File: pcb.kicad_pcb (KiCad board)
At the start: 2 copper layers, 247.4 x 96.5 mm, 170 parts, among them J0 USB_mini_micro_B, P1 CONN_3X2, P2 CONN_4, SW1.1 Backtick, SW1.10 9, SW1.11 0, SW1.12 -, SW1.13 =, SW1.2 1, SW1.3 2, SW1.4 3, SW1.5 4, SW1.6 5, SW1.7 6, SW1.8 7, SW1.9 8, SW2.1 Tab, SW2.10 I, SW2.11 O, SW2.12 P, SW2.13 /, SW2.2 Q, SW2.3 W, SW2.4 E, SW2.5 R, SW2.6 T, SW2.8 Y, SW2.9 U, SW3.1 Bksp, SW3.10 K, SW3.11 L, SW3.12 ;, SW3.13 Enter, SW3.2 A, SW3.3 S, SW3.4 D, SW3.5 F, SW3.6 G, SW3.7 B, SW3.8 H, SW3.9 J, SW4.7 Fn, SW4A1 LShift, SW4A10 ,, SW4A11 ., SW4A13 RShift, SW4A3 Z, SW4A4 X, SW4A5 C, SW4A6 V, SW4A8 N, SW4A9 M, SW4B1 LShift, SW4B10 ,, SW4B11 ., SW4B12 ., SW4B13 RShift, SW4B2 Z, SW4B3 Z, SW4B4 X, SW4B5 C, SW4B6 V, SW4B8 N, SW4B9 M, SW4C1 LShift, SW4C12 ., SW4C13 RShift, SW4C2 Z, SW5A1 LCtrl, SW5A10 1.5, SW5A12 1.5, SW5A13 1.5, SW5A2 LGUI, SW5A4 LAlt, SW5A7 Space, SW5B1 LCtrl, SW5B10 1.25, SW5B12 1.25, SW5B13 1.25, SW5B2 LGUI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

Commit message: Branch for finalizing the board.
TODO:
Swap to smaller components, finalize pads
Added footprints.pretty
Add RGB underglow
Added schematic library (keenkeeb.lib/dcm)
Remove SPI header (?)
Add test pads (?)
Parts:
- added F1: FUSE, LEDs:LED_0805, B.Cu at (94.2, 101.9)
- added LED1: WS2812b, LEDs:LED_WS2812B-PLCC4, B.Cu at (104.8, 169.1)
- added LED10: WS2812b, LEDs:LED_WS2812B-PLCC4, B.Cu at (104.8, 109.5)
- added LED2: WS2812b, LEDs:LED_WS2812B-PLCC4, B.Cu at (152.4, 169.1)
- added LED3: WS2812b, LEDs:LED_WS2812B-PLCC4, B.Cu at (200.0, 169.1)
- added LED4: WS2812b, LEDs:LED_WS2812B-PLCC4, B.Cu at (247.7, 169.1)
- added LED5: WS2812b, LEDs:LED_WS2812B-PLCC4, B.Cu at (295.3, 169.1)
- added LED6: WS2812b, LEDs:LED_WS2812B-PLCC4, B.Cu at (295.3, 109.5)
- added LED7: WS2812b, LEDs:LED_WS2812B-PLCC4, B.Cu at (247.7, 109.5)
- added LED8: WS2812b, LEDs:LED_WS2812B-PLCC4, B.Cu at (200.0, 109.5)
- added LED9: WS2812b, LEDs:LED_WS2812B-PLCC4, B.Cu at (152.4, 109.5)
- C0, C1, C2, C3, C4, C5, C6, C7: footprint Capacitors_SMD:C_0805_HandSoldering -> Capacitors_SMD:C_0805
- D1: footprint Keyboards:LED_3mm_plusminus -> footprints:LED_3mm_plusminus
- OSC0: footprint keyboard_parts:FA-238 -> footprints:OSC_EpsonFA238_SMD
- P1: moved to F.Cu
- R0, R1, R2, R3, R4: footprint Resistors_SMD:R_0805_HandSoldering -> Resistors_SMD:R_0805
- moved P1 141.3 mm to (200.0, 195.7)
- moved G3 54.7 mm to (192.3, 181.9)
- moved G2 54.5 mm to (201.7, 178.8)
- moved R2 7.85 mm to (98.1, 109.1)
- moved R1 7.77 mm to (95.0, 109.1)
- moved C3 2.97 mm to (89.6, 109.1), turned to 270 degrees
- moved C0 1.99 mm to (102.6, 116.9)
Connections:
- J0 pad 1: VCC -> Net-(F1-Pad2)
- uC0 pad 29: /matrix/Row4 -> /matrix/Row5
- uC0 pad 30: /matrix/Row5 -> /matrix/Row4
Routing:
- net VCC: track 142.7 -> 280.6 mm, vias 5 -> 13
- net Net-(LED5-Pad2): track 0.00 -> 65.1 mm, vias 0 -> 2
- net /microcontroller/MISO: track 58.7 -> 0.00 mm, vias 2 -> 0
- net /microcontroller/SCK: track 49.5 -> 0.00 mm, vias 2 -> 0
- net Net-(LED10-Pad4): track 0.00 -> 48.1 mm, vias 0 -> 2
- net /microcontroller/MOSI: track 46.8 -> 0.00 mm, vias 2 -> 0
- net Net-(LED6-Pad2): track 0.00 -> 45.9 mm, vias 0 -> 2
- net Net-(LED3-Pad2): track 0.00 -> 44.0 mm, vias 0 -> 2
- net Net-(LED2-Pad2): track 0.00 -> 44.0 mm, vias 0 -> 2
- net Net-(LED8-Pad2): track 0.00 -> 44.0 mm, vias 0 -> 2
- net Net-(LED7-Pad2): track 0.00 -> 44.0 mm, vias 0 -> 2
- net Net-(LED1-Pad2): track 0.00 -> 44.0 mm, vias 0 -> 2
- net Net-(LED4-Pad2): track 0.00 -> 44.0 mm, vias 0 -> 2
- net /microcontroller/nRST: track 72.4 -> 38.7 mm, vias 3 -> 2
- net Net-(uC0-Pad8): track 14.2 -> 0.00 mm, vias 1 -> 0
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
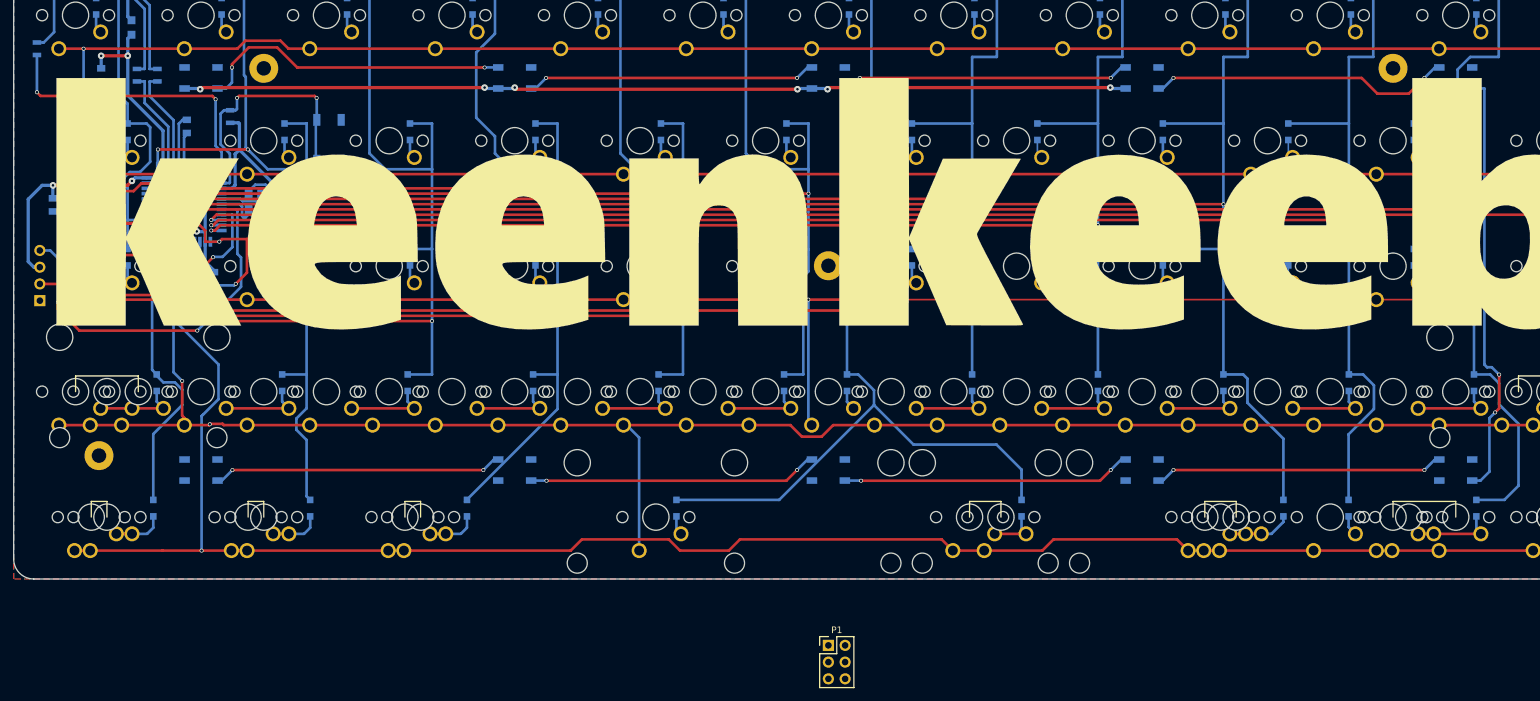
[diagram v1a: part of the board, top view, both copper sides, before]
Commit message: ARR GEE BEE!!!
Added pads for WS2812B underglow - connected to pin 11.
Rerouted some connections.
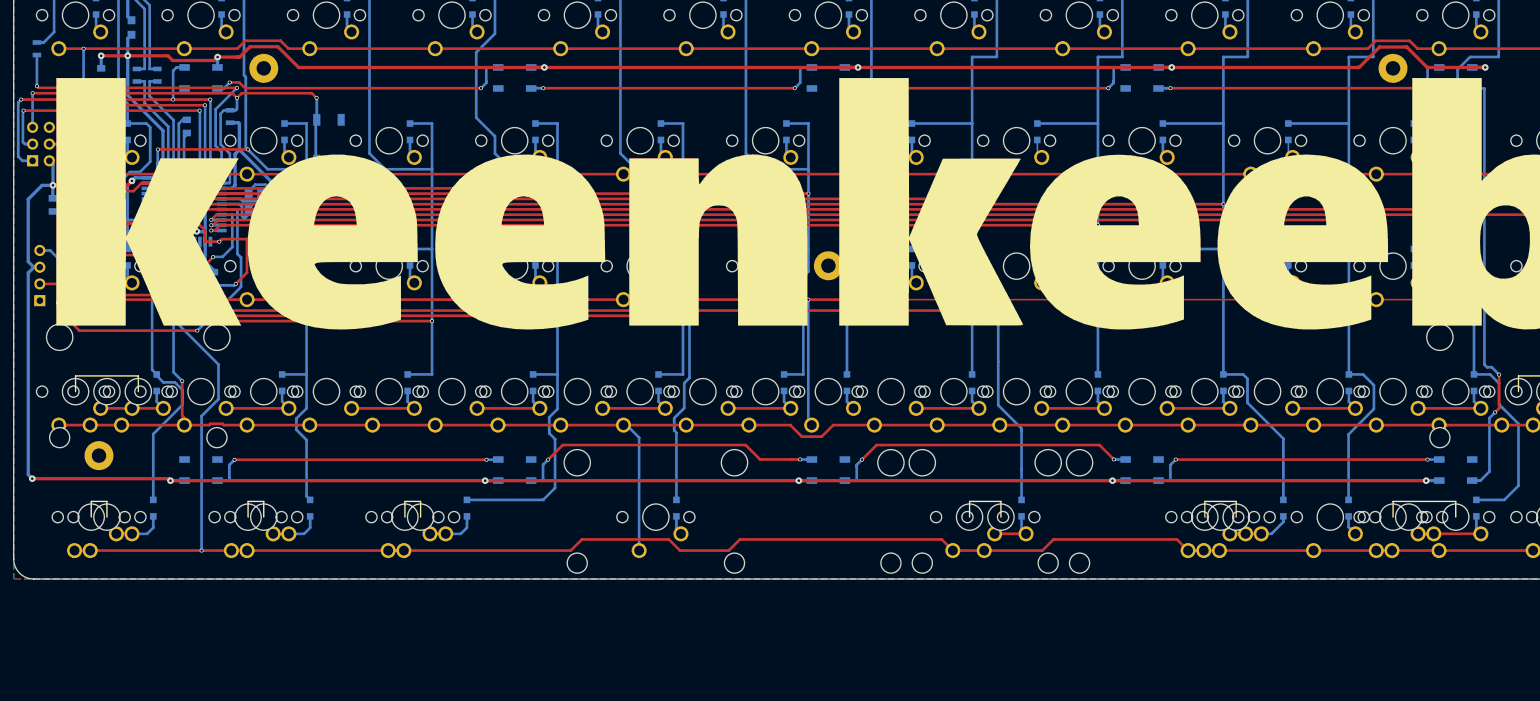
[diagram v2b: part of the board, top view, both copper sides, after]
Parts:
- P1: moved to B.Cu
- moved P1 141.5 mm to (79.2, 122.1)
- turned LED1 to 180 degrees
- turned LED10 to 0 degrees
- turned LED2 to 180 degrees
- turned LED3 to 180 degrees
- turned LED4 to 180 degrees
- turned LED5 to 180 degrees
- turned LED6 to 0 degrees
- turned LED7 to 0 degrees
- turned LED8 to 0 degrees
- turned LED9 to 0 degrees
- renumbered LED10 to LED1, LED1 to LED10, LED9 to LED2, LED8 to LED3, LED7 to LED4, LED6 to LED5, LED5 to LED6, LED4 to LED7, LED3 to LED8, LED2 to LED9
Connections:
- LED1 pad 2: Net-(LED10-Pad2) -> Net-(LED1-Pad2)
- LED1 pad 4: Net-(LED10-Pad4) -> /underglow/Din
- LED10 pad 2: Net-(LED1-Pad2) -> Net-(LED10-Pad2)
- LED10 pad 4: /underglow/Din -> Net-(LED10-Pad4)
- LED2 pad 2: Net-(LED10-Pad4) -> Net-(LED2-Pad2)
- LED2 pad 4: Net-(LED8-Pad2) -> Net-(LED1-Pad2)
- LED3 pad 2: Net-(LED8-Pad2) -> Net-(LED3-Pad2)
- LED3 pad 4: Net-(LED7-Pad2) -> Net-(LED2-Pad2)
- LED4 pad 2: Net-(LED7-Pad2) -> Net-(LED4-Pad2)
- LED4 pad 4: Net-(LED6-Pad2) -> Net-(LED3-Pad2)
- LED5 pad 2: Net-(LED6-Pad2) -> Net-(LED5-Pad2)
- LED5 pad 4: Net-(LED5-Pad2) -> Net-(LED4-Pad2)
- LED6 pad 2: Net-(LED5-Pad2) -> Net-(LED6-Pad2)
- LED6 pad 4: Net-(LED4-Pad2) -> Net-(LED5-Pad2)
- LED7 pad 2: Net-(LED4-Pad2) -> Net-(LED7-Pad2)
- LED7 pad 4: Net-(LED3-Pad2) -> Net-(LED6-Pad2)
- LED8 pad 2: Net-(LED3-Pad2) -> Net-(LED8-Pad2)
- LED8 pad 4: Net-(LED2-Pad2) -> Net-(LED7-Pad2)
- LED9 pad 2: Net-(LED2-Pad2) -> Net-(LED10-Pad4)
- LED9 pad 4: Net-(LED1-Pad2) -> Net-(LED8-Pad2)
- P1 pad 1: /microcontroller/MISO -> /underglow/Din
- uC0 pad 11: /microcontroller/MISO -> /underglow/Din
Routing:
- net VCC: track 280.6 -> 617.3 mm, vias 13 -> 18
- net /underglow/Din: track 0.00 -> 56.5 mm, vias 0 -> 3
- net /microcontroller/SCK: track 0.00 -> 41.7 mm, vias 0 -> 2
- net /microcontroller/MOSI: track 0.00 -> 38.6 mm, vias 0 -> 2
- net /microcontroller/nRST: track 38.7 -> 75.5 mm, vias 2 -> 3
- net /matrix/Col7: track 262.9 -> 253.7 mm, vias 2 -> 4
- net /matrix/Col4: track 176.2 -> 183.4 mm
- net /microcontroller/LED: track 45.5 -> 50.6 mm
- net Net-(LED8-Pad2): track 44.0 -> 47.8 mm
- net Net-(LED7-Pad2): track 44.0 -> 47.2 mm
- net Net-(LED10-Pad4): track 48.1 -> 45.3 mm
- net Net-(LED1-Pad2): track 44.0 -> 46.0 mm
- net Net-(LED3-Pad2): track 44.0 -> 45.4 mm
- net Net-(LED2-Pad2): track 44.0 -> 45.4 mm
- net Net-(LED4-Pad2): track 44.0 -> 45.3 mm
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
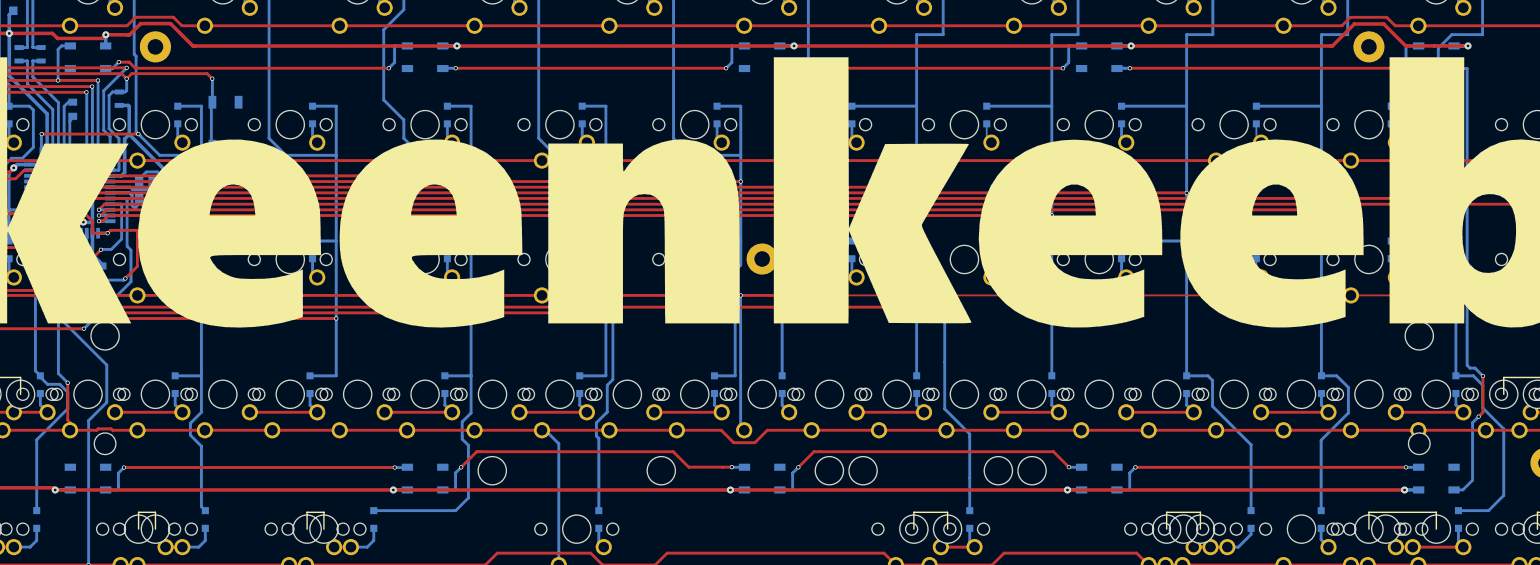
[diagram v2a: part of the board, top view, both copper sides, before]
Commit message: Added 0.1uF caps to LEDs
Added capacitors from Vcc to GND for WS2812s
Also changed some references
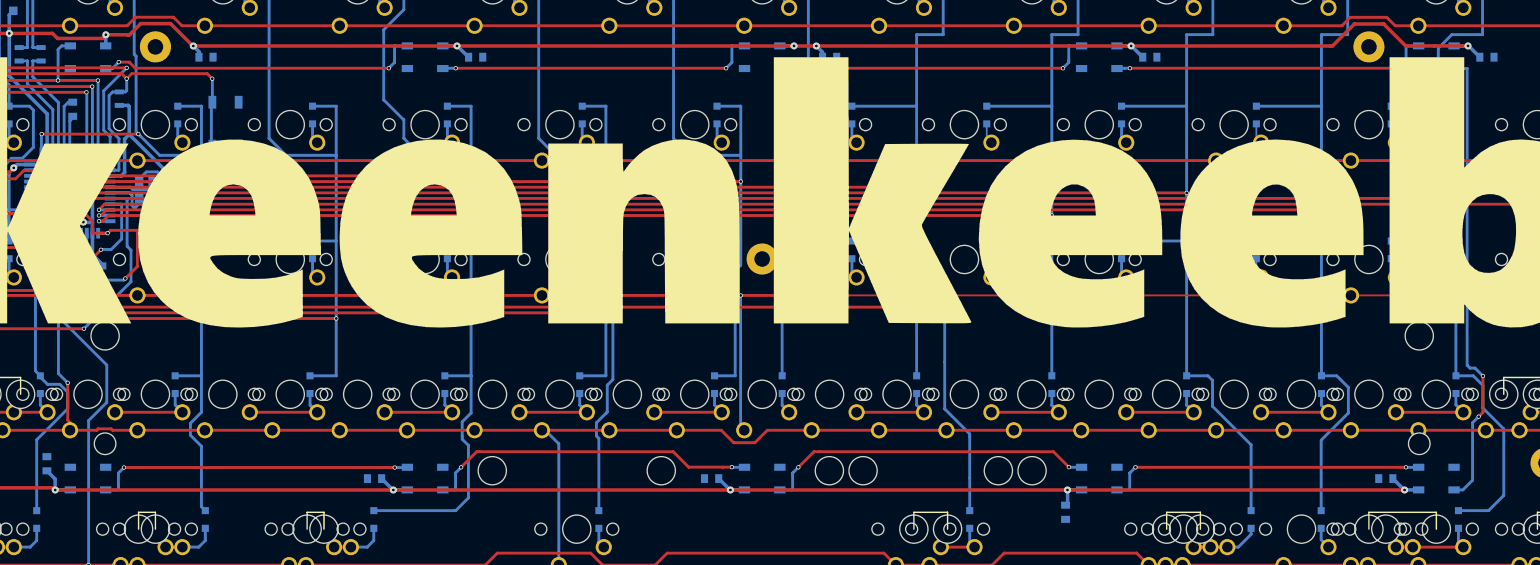
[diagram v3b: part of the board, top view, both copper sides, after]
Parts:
- added C10: 0.1u, Capacitors_SMD:C_0805, B.Cu at (159.5, 109.5)
- added C11: 0.1u, Capacitors_SMD:C_0805, B.Cu at (209.6, 109.5)
- added C12: 0.1u, Capacitors_SMD:C_0805, B.Cu at (254.8, 109.5)
- added C13: 0.1u, Capacitors_SMD:C_0805, B.Cu at (302.4, 109.5)
- added C14: 0.1u, Capacitors_SMD:C_0805, B.Cu at (288.1, 169.1)
- added C15: 0.1u, Capacitors_SMD:C_0805, B.Cu at (242.9, 173.8)
- added C16: 0.1u, Capacitors_SMD:C_0805, B.Cu at (192.9, 169.1)
- added C17: 0.1u, Capacitors_SMD:C_0805, B.Cu at (145.3, 169.1)
- added C18: 0.1u, Capacitors_SMD:C_0805, B.Cu at (99.0, 167.0)
- added C9: 0.1u, Capacitors_SMD:C_0805, B.Cu at (121.4, 109.5)
- renumbered C0 to C1, C1 to C2, C2 to C3, C3 to C4, C4 to C5, C5 to C6, C6 to C7, C7 to C8, R0 to R3, R3 to R4, R4 to R5, uC0 to U1
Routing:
- net VCC: track 617.3 -> 640.6 mm, vias 18 -> 20

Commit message: Moved some of the footprints around.
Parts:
- moved PB0 21.1 mm to (114.7, 100.2), turned to 270 degrees
- moved C9 11.8 mm to (109.8, 107.6), turned to 90 degrees
- moved C7 5.31 mm to (90.4, 128.8)
- moved C15 4.91 mm to (242.0, 169.0), turned to 0 degrees
- moved C11 3.78 mm to (205.8, 109.6)
- moved C18 2.16 mm to (99.1, 169.1), turned to 0 degrees
- moved C16 1.46 mm to (194.3, 169.0)
- moved C17 1.46 mm to (146.7, 169.0)
- moved C14 1.46 mm to (289.6, 169.1)
- moved C10 1.40 mm to (158.1, 109.6)
- moved C12 1.40 mm to (253.4, 109.6)
- moved C13 1.40 mm to (301.0, 109.6)
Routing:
- net VCC: track 640.6 -> 628.3 mm, vias 20 -> 18
- net GND: track 96.5 -> 104.5 mm
- net /matrix/Col8: track 208.3 -> 206.1 mm
- net /matrix/Col9: track 219.7 -> 217.5 mm
- net /matrix/Col11: track 281.3 -> 279.1 mm
- net /matrix/Col12: track 314.3 -> 312.1 mm
- net /matrix/Col10: track 278.7 -> 276.5 mm
- net /matrix/Col13: track 313.1 -> 312.2 mm
- net /microcontroller/nRST: track 75.5 -> 76.4 mm
- net /matrix/Col1: track 99.8 -> 100.4 mm

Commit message: Begun work for rev 1 layout, which supports ortholinear rows 2 and 3.
Converted all switches to use platemount footprint.  Added additional
set of switches to row 3 for a completely ortholinear layout.
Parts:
- removed SW3.1: Bksp, Keyboards:CHERRY_PCB_150H_NoBound
- removed SW3.10: K, Keyboards:CHERRY_PCB_100H_NoBound
- removed SW3.11: L, Keyboards:CHERRY_PCB_100H_NoBound
- removed SW3.12: ;, Keyboards:CHERRY_PCB_100H_NoBound
- removed SW3.13: Enter, Keyboards:CHERRY_PCB_150H_NoBound
- removed SW3.2: A, Keyboards:CHERRY_PCB_100H_NoBound
- removed SW3.3: S, Keyboards:CHERRY_PCB_100H_NoBound
- removed SW3.4: D, Keyboards:CHERRY_PCB_100H_NoBound
- removed SW3.5: F, Keyboards:CHERRY_PCB_100H_NoBound
- removed SW3.6: G, Keyboards:CHERRY_PCB_100H_NoBound
- removed SW3.7: B, Keyboards:CHERRY_PCB_100H_NoBound
- removed SW3.8: H, Keyboards:CHERRY_PCB_100H_NoBound
- removed SW3.9: J, Keyboards:CHERRY_PCB_100H_NoBound
- added SW3A1: Bksp, footprints:MX_150_Plate, F.Cu at (90.5, 138.1)
- added SW3A10: K, footprints:MX_100_Plate, F.Cu at (247.7, 138.1)
- added SW3A11: L, footprints:MX_100_Plate, F.Cu at (266.7, 138.1)
- added SW3A12: ;, footprints:MX_100_Plate, F.Cu at (285.8, 138.1)
- added SW3A13: Enter, footprints:MX_150_Plate, F.Cu at (309.6, 138.1)
- added SW3A2: A, footprints:MX_100_Plate, F.Cu at (114.3, 138.1)
- added SW3A3: S, footprints:MX_100_Plate, F.Cu at (133.3, 138.1)
- added SW3A4: D, footprints:MX_100_Plate, F.Cu at (152.4, 138.1)
- added SW3A5: F, footprints:MX_100_Plate, F.Cu at (171.4, 138.1)
- added SW3A6: G, footprints:MX_100_Plate, F.Cu at (190.5, 138.1)
- added SW3A8: H, footprints:MX_100_Plate, F.Cu at (209.6, 138.1)
- added SW3A9: J, footprints:MX_100_Plate, F.Cu at (228.6, 138.1)
- added SW3B7: B, footprints:MX_100_Plate, F.Cu at (200.0, 138.1)
- SW1.1, SW1.10, SW1.11, SW1.12, SW1.13, SW1.2, SW1.3, SW1.4, SW1.5, SW1.6, SW1.7, SW1.8, SW1.9, SW2.10, SW2.11, SW2.12, SW2.2, SW2.3, SW2.4, SW2.5, SW2.6, SW2.8, SW2.9, SW4A10, SW4A11, SW4A3, SW4A4, SW4A5, SW4A6, SW4A8, SW4A9, SW4B10, SW4B11, SW4B12, SW4B2, SW4B3, SW4B4, SW4B5, SW4B6, SW4B8, SW4B9, SW4C1, SW4C12, SW4C13, SW4C2, SW5A12, SW5A2, SW5C10, SW5C11, SW5C12, SW5C13: footprint Keyboards:CHERRY_PCB_100H_NoBound -> footprints:MX_100_Plate
- SW2.1, SW2.13, SW4B1, SW5A1, SW5A10, SW5A13, SW5A4: footprint Keyboards:CHERRY_PCB_150H_NoBound -> footprints:MX_150_Plate
- SW4.7: footprint Keyboards:CHERRY_PCB_225H_NoBound -> footprints:MX_225_Plate
- SW4A1, SW4A13: footprint Keyboards:CHERRY_PCB_200H_NoBound -> footprints:MX_200_Plate
- SW4B13: footprint Keyboards:CHERRY_PCB_100H_NoBound -> footprints:MX_150_Plate
- SW5A7, SW5B7: footprint Keyboards:CHERRY_PCB_275H_NoBound -> footprints:MX_275_Plate
- SW5B1, SW5B10, SW5B12, SW5B13, SW5B2, SW5B4: footprint Keyboards:CHERRY_PCB_125H_NoBound -> footprints:MX_125_Plate
- moved C13 303.0 mm to (37.9, 259.9)
- moved LED5 295.3 mm to (36.9, 252.6)
- moved Hole5 280.3 mm to (30.6, 177.3)
- moved C8 275.0 mm to (356.4, 106.8)
- moved C12 274.8 mm to (24.1, 261.0)
- moved LED6 269.0 mm to (29.4, 209.9)
- moved R4 265.4 mm to (362.9, 111.6)
- moved LED4 265.2 mm to (24.3, 252.6)
- moved C14 264.5 mm to (29.2, 215.7)
- moved C7 262.9 mm to (352.3, 106.5)
- moved C4 260.4 mm to (350.0, 111.0)
- moved C3 258.9 mm to (372.5, 104.2), turned to 90 degrees
- moved Hole2 258.7 mm to (31.4, 155.5)
- moved OSC0 253.0 mm to (364.8, 103.7), turned to 0 degrees
- moved C2 247.2 mm to (363.0, 97.1)
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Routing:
- net VCC: track 628.3 -> 17.4 mm, vias 18 -> 0
- net /matrix/Col13: track 312.2 -> 97.3 mm, vias 2 -> 0
- net /matrix/Col12: track 312.1 -> 110.2 mm, vias 2 -> 0
- net /matrix/Col11: track 279.1 -> 104.5 mm, vias 2 -> 0
- net /matrix/Col10: track 276.5 -> 112.6 mm, vias 2 -> 0
- net /matrix/Col9: track 217.5 -> 81.0 mm, vias 2 -> 0
- net /matrix/Col8: track 206.1 -> 80.4 mm, vias 2 -> 0
- net /matrix/Col6: track 186.4 -> 85.6 mm, vias 2 -> 0
- net GND: track 104.5 -> 4.10 mm, vias 6 -> 0
- net /matrix/Col7: track 253.7 -> 158.7 mm, vias 4 -> 3
- net /matrix/Col5: track 171.4 -> 86.0 mm, vias 2 -> 0
- net /microcontroller/nRST: track 76.4 -> 0.00 mm, vias 3 -> 0
- net Net-(LED5-Pad2): track 65.1 -> 0.00 mm, vias 2 -> 0
- net /matrix/Col4: track 183.4 -> 120.6 mm, vias 2 -> 0
- net /microcontroller/SCL: track 57.1 -> 0.00 mm, vias 2 -> 0
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
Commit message: Ortholinear switch footprints added to row 2.
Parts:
- added D2.7: D, Diodes_SMD:D_SOD-323_HandSoldering, B.Cu at (204.8, 116.7)
- added SW2B1: Tab, footprints:MX_100_Plate, F.Cu at (85.7, 119.1)
- added SW2B10: I, footprints:MX_100_Plate, F.Cu at (257.2, 119.1)
- added SW2B11: O, footprints:MX_100_Plate, F.Cu at (276.2, 119.1)
- added SW2B12: P, footprints:MX_100_Plate, F.Cu at (295.3, 119.1)
- added SW2B13: /, footprints:MX_100_Plate, F.Cu at (314.3, 119.1)
- added SW2B2: Q, footprints:MX_100_Plate, F.Cu at (104.8, 119.1)
- added SW2B3: W, footprints:MX_100_Plate, F.Cu at (123.8, 119.1)
- added SW2B4: E, footprints:MX_100_Plate, F.Cu at (142.9, 119.1)
- added SW2B5: R, footprints:MX_100_Plate, F.Cu at (161.9, 119.1)
- added SW2B6: T, footprints:MX_100_Plate, F.Cu at (181.0, 119.1)
- added SW2B7: Y, footprints:MX_100_Plate, F.Cu at (200.0, 119.1)
- added SW2B8: Y, footprints:MX_100_Plate, F.Cu at (219.1, 119.1)
- added SW2B9: U, footprints:MX_100_Plate, F.Cu at (238.1, 119.1)
- added SW3B1: Bksp, footprints:MX_100_Plate, F.Cu at (85.7, 138.1)
- added SW3B10: K, footprints:MX_100_Plate, F.Cu at (257.2, 138.1)
- added SW3B11: L, footprints:MX_100_Plate, F.Cu at (276.2, 138.1)
- added SW3B12: ;, footprints:MX_100_Plate, F.Cu at (295.3, 138.1)
- added SW3B13: Enter, footprints:MX_100_Plate, F.Cu at (314.3, 138.1)
- added SW3B2: A, footprints:MX_100_Plate, F.Cu at (104.8, 138.1)
- added SW3B3: S, footprints:MX_100_Plate, F.Cu at (123.8, 138.1)
- added SW3B4: D, footprints:MX_100_Plate, F.Cu at (142.9, 138.1)
- added SW3B5: F, footprints:MX_100_Plate, F.Cu at (161.9, 138.1)
- added SW3B6: G, footprints:MX_100_Plate, F.Cu at (181.0, 138.1)
- added SW3B8: H, footprints:MX_100_Plate, F.Cu at (219.1, 138.1)
- added SW3B9: J, footprints:MX_100_Plate, F.Cu at (238.1, 138.1)
- SW3B7: value B -> H
- moved Hole5 272.1 mm to (302.4, 190.5)
- moved Hole2 265.1 mm to (285.8, 81.0)
- moved Hole1 106.8 mm to (114.3, 81.0)
- moved Hole4 72.6 mm to (100.0, 192.9)
- renumbered SW2.1 to SW2A1, SW2.10 to SW2A10, SW2.11 to SW2A11, SW2.12 to SW2A12, SW2.13 to SW2A13, SW2.2 to SW2A2, SW2.3 to SW2A3, SW2.4 to SW2A4, SW2.5 to SW2A5, SW2.6 to SW2A6, SW2.8 to SW2A8, SW2.9 to SW2A9
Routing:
- net /matrix/Row3: track 238.3 -> 0.00 mm, vias 1 -> 0
- net /matrix/Col7: track 158.7 -> 0.00 mm, vias 3 -> 0
- net /matrix/Col4: track 120.6 -> 0.00 mm
- net /matrix/Col10: track 112.6 -> 0.00 mm
- net /matrix/Col12: track 110.2 -> 0.00 mm
- net /matrix/Col2: track 105.9 -> 0.00 mm
- net /matrix/Col11: track 104.5 -> 0.00 mm
- net /matrix/Col1: track 97.5 -> 0.00 mm
- net /matrix/Col13: track 97.3 -> 0.00 mm
- net /matrix/Col5: track 86.0 -> 0.00 mm
- net /matrix/Col3: track 86.0 -> 0.00 mm
- net /matrix/Col6: track 85.6 -> 0.00 mm
- net /matrix/Col9: track 81.0 -> 0.00 mm
- net /matrix/Col8: track 80.4 -> 0.00 mm
- net /matrix/Row4: track 259.9 -> 239.7 mm
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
